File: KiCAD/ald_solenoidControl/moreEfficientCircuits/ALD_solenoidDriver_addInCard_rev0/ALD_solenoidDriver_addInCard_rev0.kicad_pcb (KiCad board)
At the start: 2 copper layers, 50 x 40 mm, 10 parts, among them U1 ASSR-1611

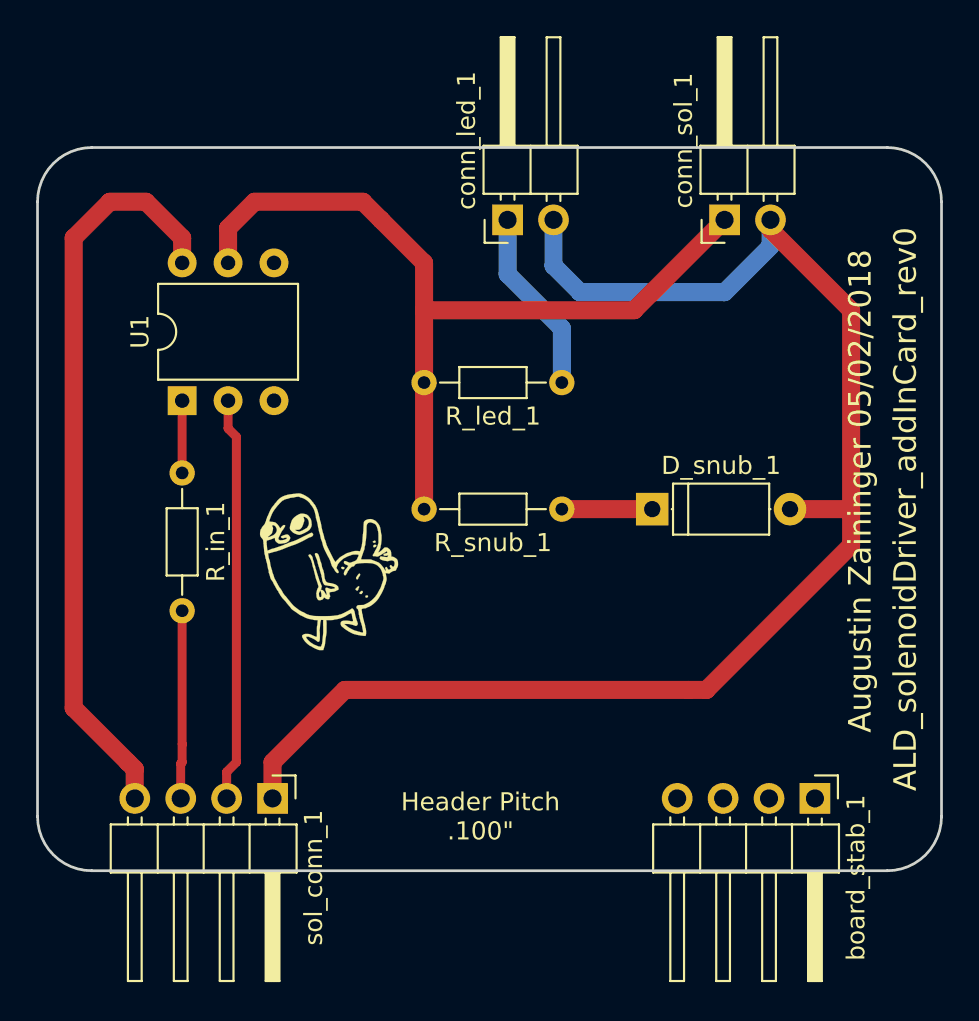
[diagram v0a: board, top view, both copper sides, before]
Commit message: add mounting holes to add in card, make zones, move current limiting resistor
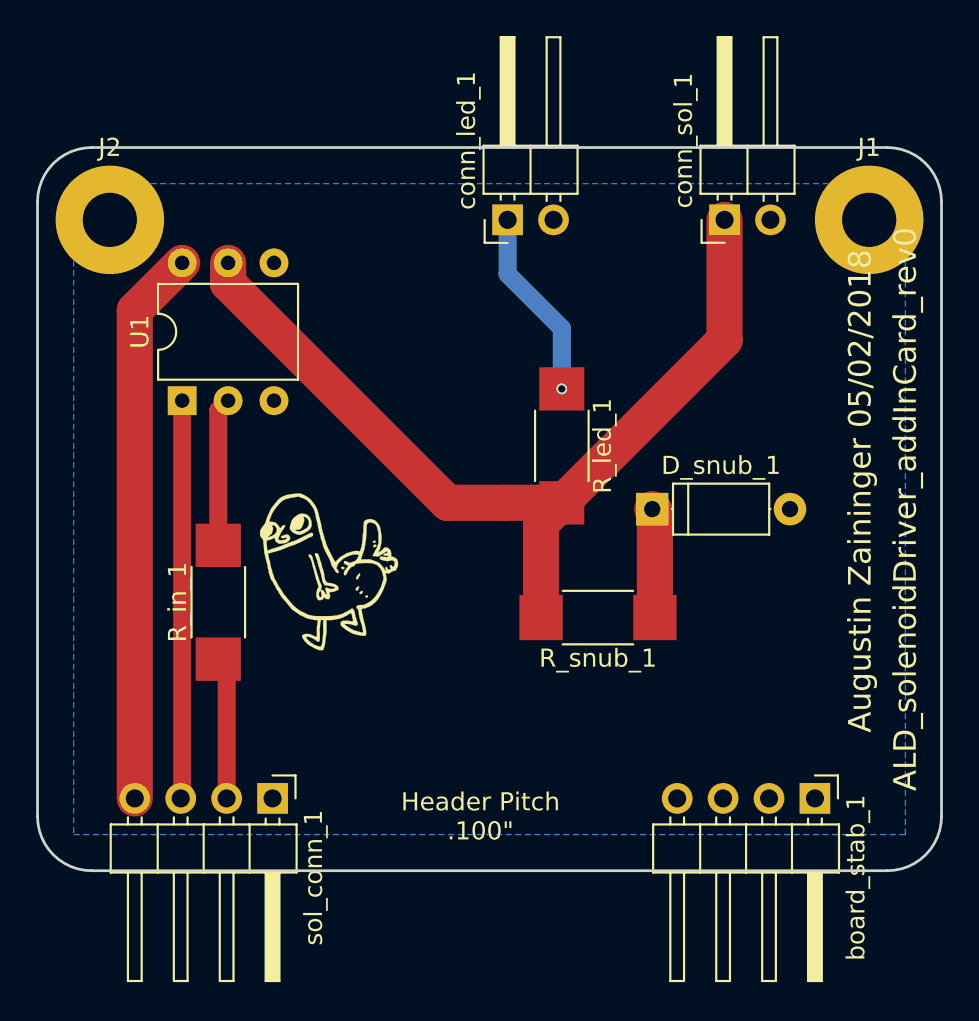
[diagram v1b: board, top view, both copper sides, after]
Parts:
- added J1: Conn_01x01, Mounting_Holes:MountingHole_3mm_Pad, F.Cu at (111.0, 84.0)
- added J2: Conn_01x01, Mounting_Holes:MountingHole_3mm_Pad, F.Cu at (69.0, 84.0)
- R_in_1, R_led_1, R_snub_1: footprint Resistors_THT:R_Axial_DIN0204_L3.6mm_D1.6mm_P7.62mm_Horizontal -> Resistors_SMD:R_2010_HandSoldering
- moved R_in_1 7.42 mm to (75.0, 105.2), turned to 90 degrees
- moved R_snub_1 6.32 mm to (96.0, 106.0)
- moved R_led_1 3.50 mm to (94.0, 96.5), turned to 270 degrees
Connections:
- R_in_1 pad 1: Net-(R_in_1-Pad1) -> signal_gnd
- R_in_1 pad 2: signal_in -> Net-(R_in_1-Pad2)
- U1 pad 1: Net-(R_in_1-Pad1) -> signal_in
- U1 pad 2: signal_gnd -> Net-(R_in_1-Pad2)
- U1 pad 3: Net-(U1-Pad3) -> (no net)
- U1 pad 4: Net-(U1-Pad4) -> (no net)
- board_stab_1 pad 1: Net-(board_stab_1-Pad1) -> (no net)
- board_stab_1 pad 2: Net-(board_stab_1-Pad2) -> (no net)
- board_stab_1 pad 3: Net-(board_stab_1-Pad3) -> (no net)
- board_stab_1 pad 4: Net-(board_stab_1-Pad4) -> (no net)
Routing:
- net GNDPWR: track 79.9 -> 0.00 mm
- net signal_gnd: track 22.4 -> 7.89 mm
- net signal_in: track 10.4 -> 22.0 mm
- net +24V: track 41.4 -> 30.7 mm
- net Net-(R_in_1-Pad2): track 0.00 -> 8.22 mm
- net Net-(R_in_1-Pad1): track 4.00 -> 0.00 mm
- net optoIsolator_out: track 47.1 -> 50.8 mm
- net Net-(D_snub_1-Pad1): track 5.00 -> 6.06 mm
- net Net-(R_led_1-Pad1): track 10.2 -> 10.6 mm, vias 0 -> 1
- added copper zone on B.Cu, net GNDPWR

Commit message: random mods
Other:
- board text added: "Augustin Zaininger 022ff63"
- board text removed: "Augustin Zaininger 05/02/2018"
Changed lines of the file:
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@@
     (links 12)
     (no_connects 0)
-    (area 64.924999 79.924999 115.075001 120.075001)
+    (area 64.252381 73.224999 115.74762 126.775001)
     (thickness 1.6)
     (drawings 11)
@@
     (visible_elements 7FFFFFFF)
     (pcbplotparams
-      (layerselection 0x00030_80000001)
+      (layerselection 0x010fc_80000001)
       (usegerberextensions false)
       (excludeedgelayer true)
@@
       (outputformat 1)
       (mirror false)
-      (drillshape 1)
+      (drillshape 0)
       (scaleselection 1)
-      (outputdirectory ""))
+      (outputdirectory output/))
   )
   (net 0 "")
@@
     (descr "Through hole angled pin header, 1x04, 2.54mm pitch, 6mm pin length, single row")
     (tags "Through hole angled pin header THT 1x04 2.54mm single row")
-    (fp_text reference sol_conn_1 (at 4.385 -2.27 270) (layer F.SilkS)
+    (fp_text reference sol_conn_1 (at 4.385 -2.27 270) (layer F.SilkS) hide
       (effects (font (size 1 1) (thickness 0.15)))
     )
@@
     (descr "Through hole angled pin header, 1x04, 2.54mm pitch, 6mm pin length, single row")
     (tags "Through hole angled pin header THT 1x04 2.54mm single row")
-    (fp_text reference board_stab_1 (at 4.385 -2.27 270) (layer F.SilkS)
+    (fp_text reference board_stab_1 (at 4.385 -2.27 270) (layer F.SilkS) hide
       (effects (font (size 1 1) (thickness 0.15)))
     )
@@
     (descr "Through hole angled pin header, 1x02, 2.54mm pitch, 6mm pin length, single row")
     (tags "Through hole angled pin header THT 1x02 2.54mm single row")
-    (fp_text reference conn_led_1 (at 4.385 -2.27 90) (layer F.SilkS)
+    (fp_text reference conn_led_1 (at -3 1 180) (layer F.SilkS)
       (effects (font (size 1 1) (thickness 0.15)))
     )
@@
     (descr "Through hole angled pin header, 1x02, 2.54mm pitch, 6mm pin length, single row")
     (tags "Through hole angled pin header THT 1x02 2.54mm single row")
-    (fp_text reference conn_sol_1 (at 4.385 -2.27 90) (layer F.SilkS)
+    (fp_text reference conn_sol_1 (at -3 1 180) (layer F.SilkS)
       (effects (font (size 1 1) (thickness 0.15)))
     )
@@
     (tags "mounting hole 3mm")
     (attr virtual)
-    (fp_text reference J1 (at 0 -4) (layer F.SilkS)
+    (fp_text reference J1 (at 0 -4) (layer F.SilkS) hide
       (effects (font (size 1 1) (thickness 0.15)))
     )
@@
     (tags "mounting hole 3mm")
     (attr virtual)
-    (fp_text reference J2 (at 0 -4) (layer F.SilkS)
+    (fp_text reference J2 (at 0 -4) (layer F.SilkS) hide
       (effects (font (size 1 1) (thickness 0.15)))
     )
@@
     (effects (font (size 1 1) (thickness 0.2)))
   )
-  (gr_text "Augustin Zaininger 05/02/2018" (at 110.5 99 90) (layer F.SilkS)
+  (gr_text "Augustin Zaininger 022ff63" (at 110.5 102 90) (layer F.SilkS)
     (effects (font (size 1.25 1.25) (thickness 0.25)))
   )
@@
   (gr_line (start 68 120) (end 112 120) (angle 90) (layer Edge.Cuts) (width 0.15))
   (gr_line (start 68 80) (end 112 80) (angle 90) (layer Edge.Cuts) (width 0.15))
-  (gr_text ALD_solenoidDriver_addInCard_rev0 (at 113 100 90) (layer F.SilkS)
+  (gr_text ALD_solenoidDriver_addInCard_rev0 (at 113 103 90) (layer F.SilkS)
     (effects (font (size 1.25 1.25) (thickness 0.25)))
   )
